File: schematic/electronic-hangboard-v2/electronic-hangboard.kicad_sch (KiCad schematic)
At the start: 47 parts, among them J2 Conn_01x04_Pin, J3 JTAG, J4 Conn_01x01_Pin, J5 UART, J6 Conn_01x01_Pin, Q1 S9015, U1 ESP32-WROOM-32, U2 HX711, U3 MT3608, U4 AMS1117-3.3

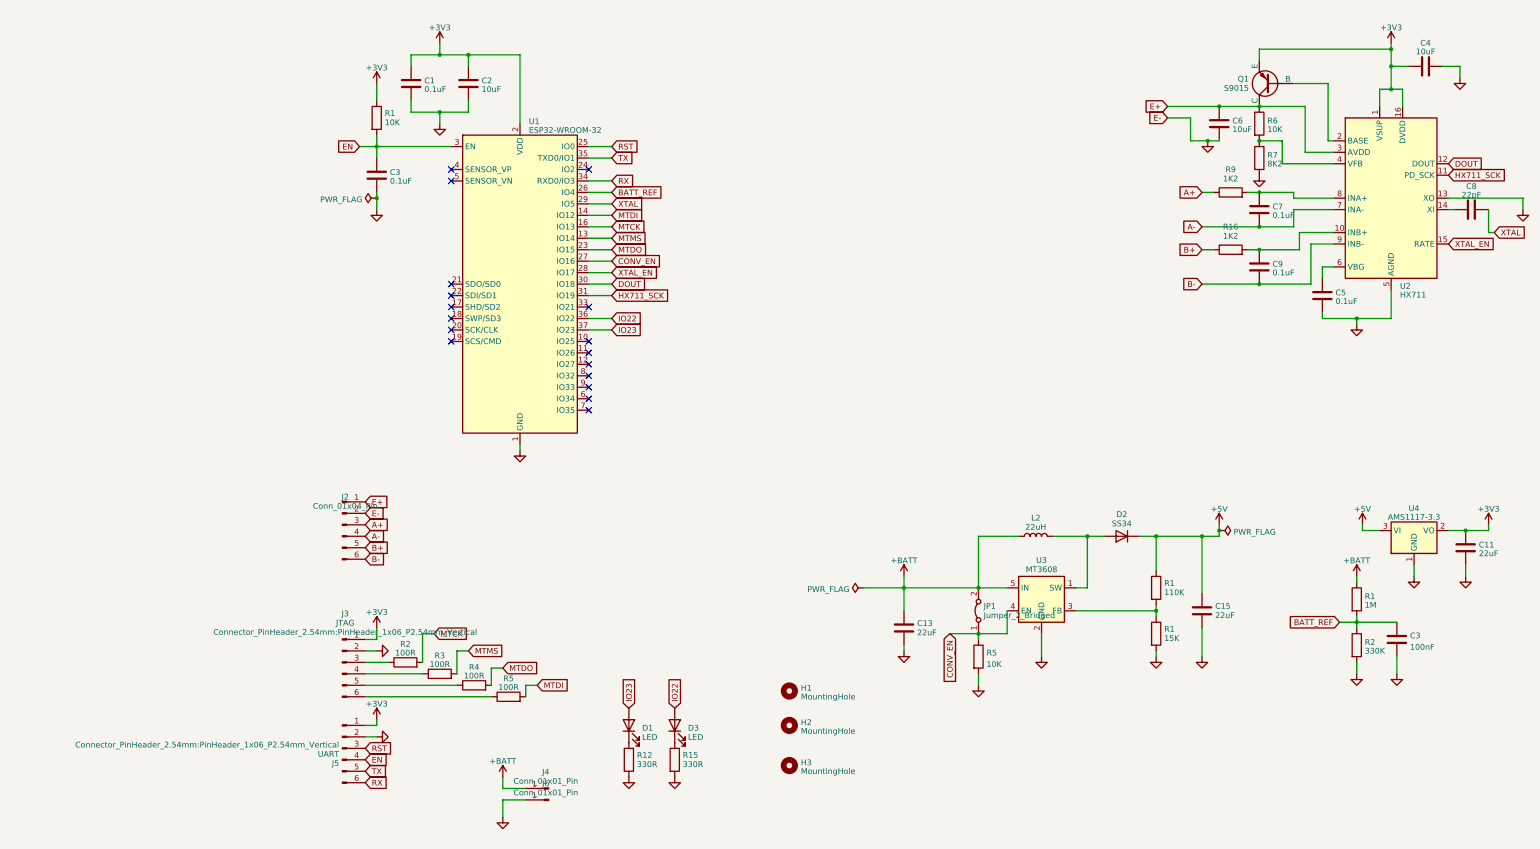
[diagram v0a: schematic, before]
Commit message: add firmware and some hardware documentation
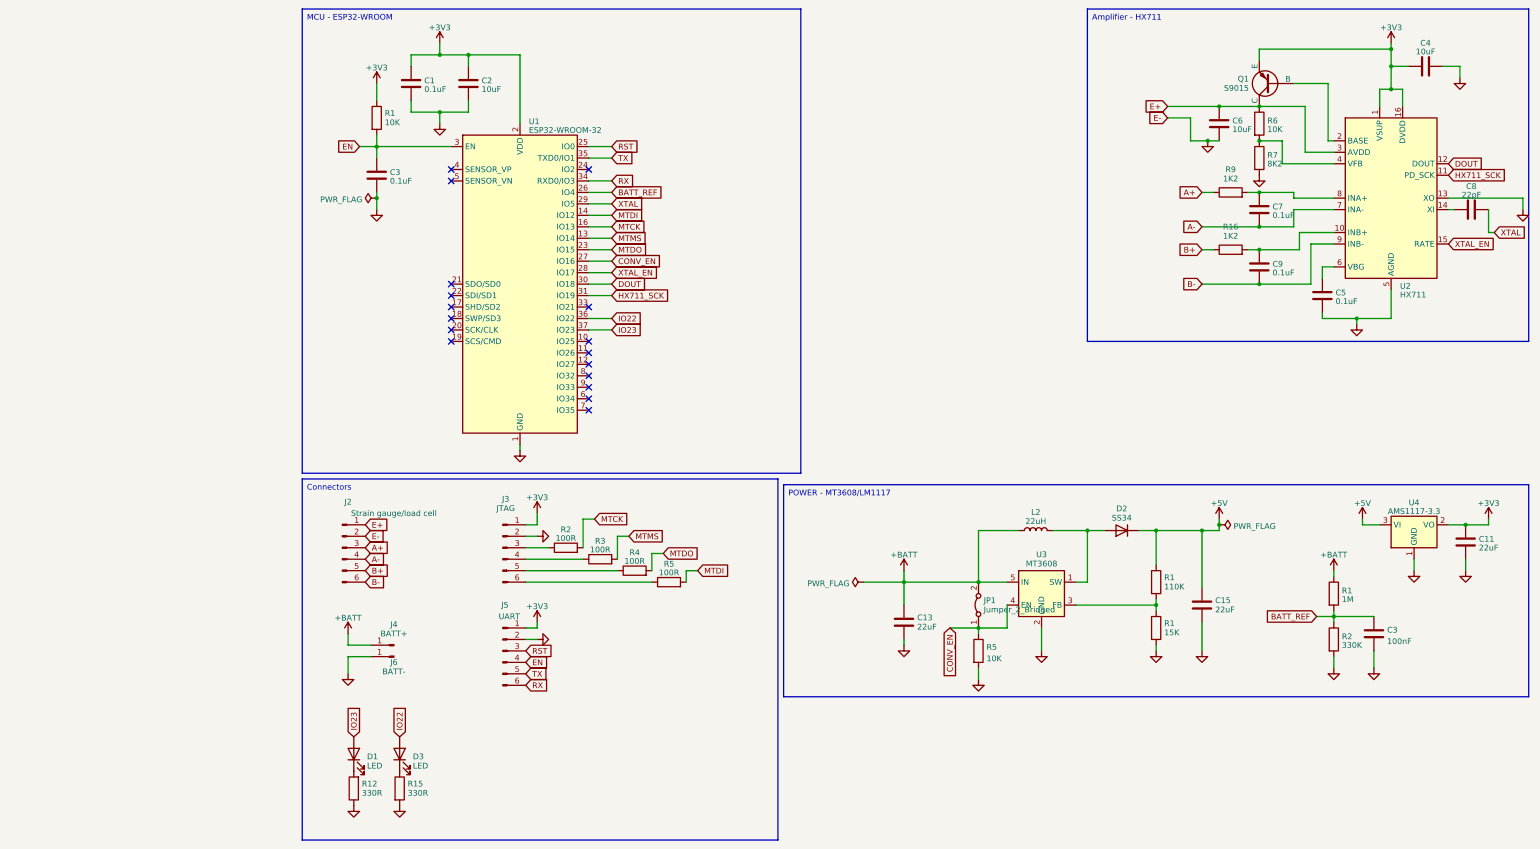
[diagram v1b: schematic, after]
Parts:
- removed H1, H2, H3: MountingHole, MountingHole:MountingHole_3.2mm_M3_DIN965_Pad_TopBottom, symbol Mechanical:MountingHole
- J2: value Conn_01x04_Pin -> Strain gauge/load cell
- J4: value Conn_01x01_Pin -> BATT+
- J6: value Conn_01x01_Pin -> BATT-
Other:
- moved on the sheet: C11, C13, C15, C3, D1, D2, D3, J2, J3, J4, J5, J6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
